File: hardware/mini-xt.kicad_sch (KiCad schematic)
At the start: 0 parts

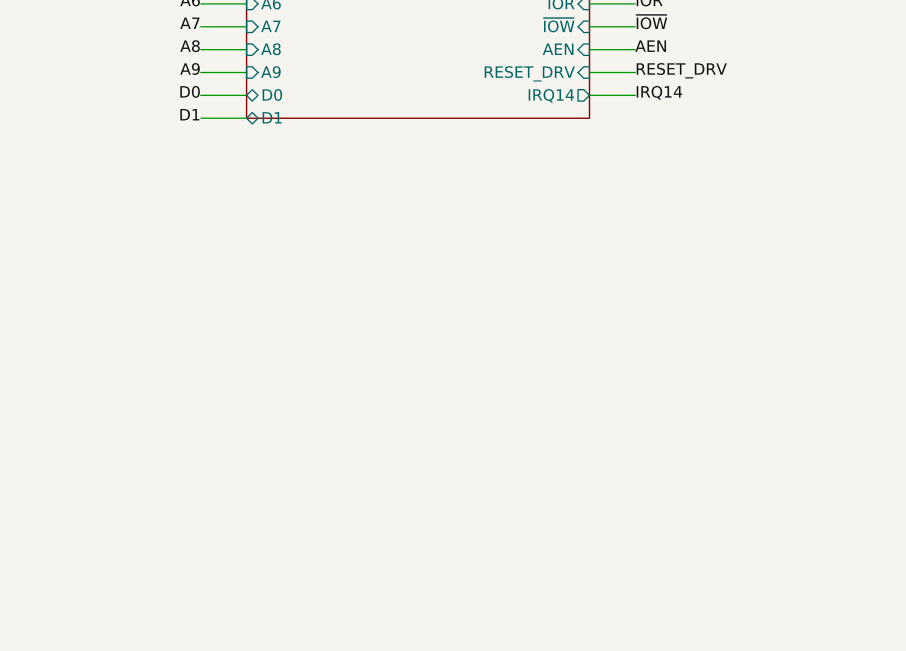
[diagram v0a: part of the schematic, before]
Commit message: Build: register network sheet; parts.py NIC bindings
Wire the RTL8019AS NIC sheet (Task 2) into build.py's SHEETS list and
bind its five new parts (RTL8019AS, AT93C46, 13F-39MNL, RJ45_LED, 20MHz
crystal) plus five newly-needed passive values (27k/1M/200 resistors,
20pF/1nF caps) in parts.py. Full rebuild: root + 13 sheets, 0 structural
ERC violations (1 expected pin_to_pin on the IOCHRDY wired-AND, matching
CLAUDE.md's ignorable categories). IRQ2 and IOCHRDY nets confirmed to
span network + the other soft cards in the regenerated netlist.
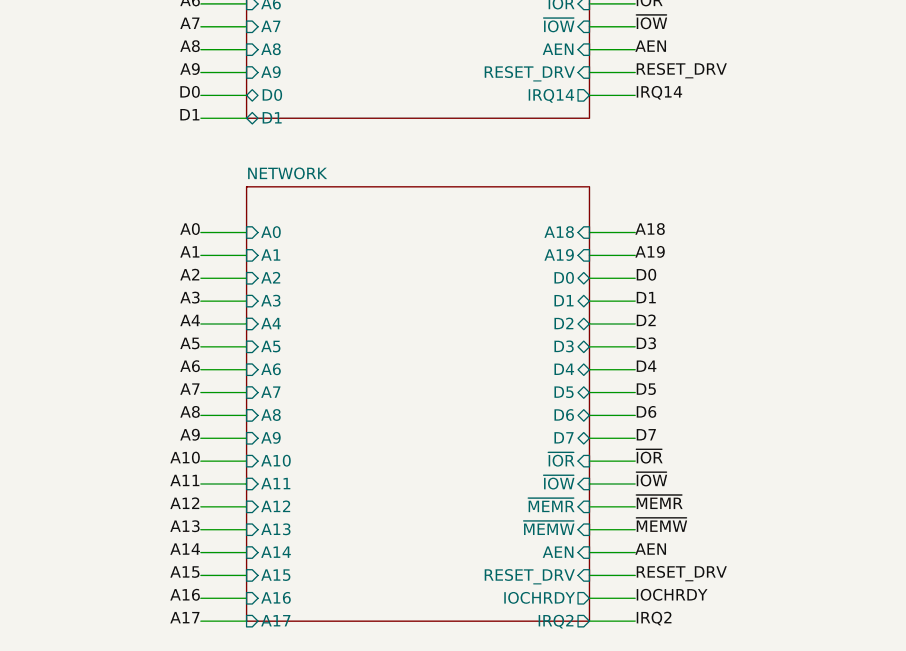
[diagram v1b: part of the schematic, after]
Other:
- added sheet NETWORK (sheets/network.kicad_sch)
